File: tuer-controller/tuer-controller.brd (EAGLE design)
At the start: 46.7 x 43.2 mm, 19 parts, among them IC1 ATTINY24/44/84-PU

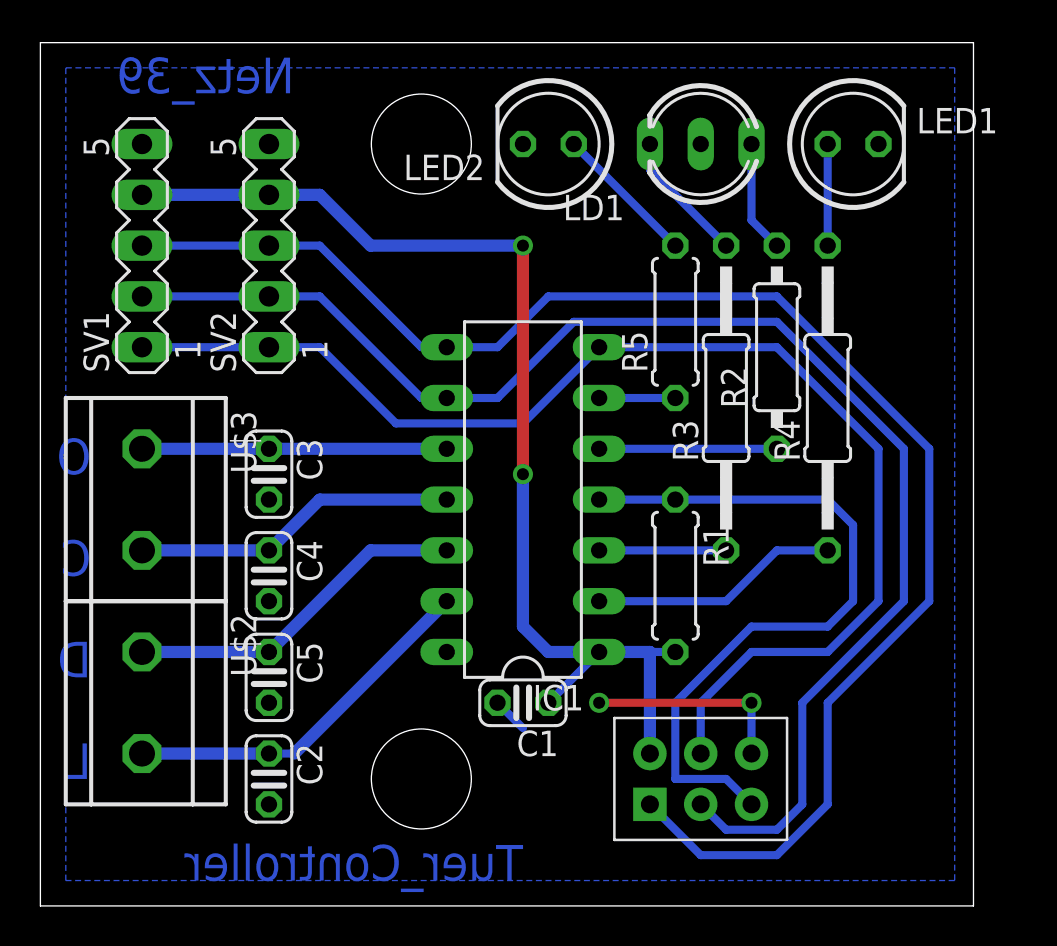
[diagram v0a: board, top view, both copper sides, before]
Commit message: Mindesgrößen der Pads und Vias angepasst
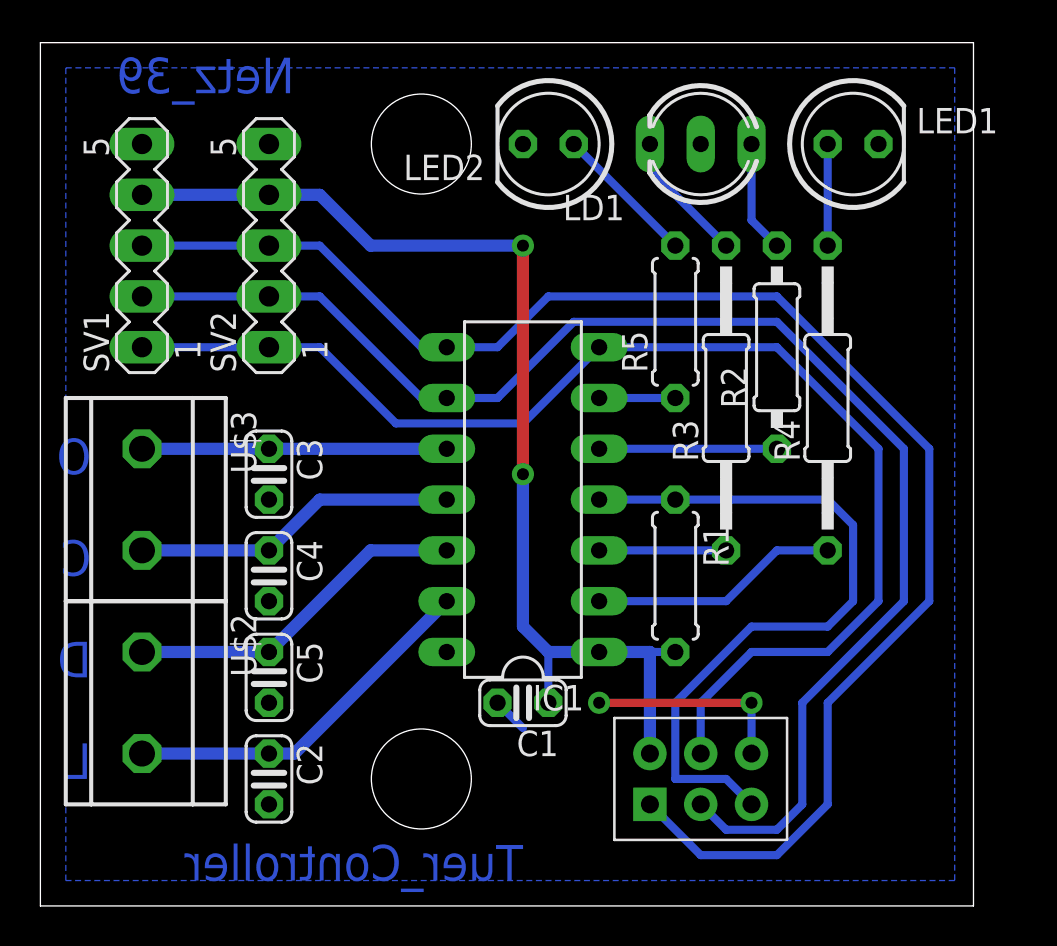
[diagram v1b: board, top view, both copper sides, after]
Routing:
- net VCC: track 56.0 -> 54.9 mm
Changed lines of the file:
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@@
 </class>
 </classes>
-<designrules name="default">
+<designrules name="default *">
 <description language="de">&lt;b&gt;EAGLE Design Rules&lt;/b&gt;
 &lt;p&gt;
@@
 <param name="mdDrill" value="8mil"/>
 <param name="mdSmdStop" value="0mil"/>
-<param name="msWidth" value="10mil"/>
+<param name="msWidth" value="12mil"/>
 <param name="msDrill" value="24mil"/>
 <param name="msMicroVia" value="9.99mm"/>
@@
 <param name="rvMicroViaOuter" value="0.25"/>
 <param name="rvMicroViaInner" value="0.25"/>
-<param name="rlMinPadTop" value="10mil"/>
+<param name="rlMinPadTop" value="12mil"/>
 <param name="rlMaxPadTop" value="20mil"/>
-<param name="rlMinPadInner" value="10mil"/>
+<param name="rlMinPadInner" value="12mil"/>
 <param name="rlMaxPadInner" value="20mil"/>
-<param name="rlMinPadBottom" value="10mil"/>
+<param name="rlMinPadBottom" value="12mil"/>
 <param name="rlMaxPadBottom" value="20mil"/>
-<param name="rlMinViaOuter" value="8mil"/>
+<param name="rlMinViaOuter" value="10mil"/>
 <param name="rlMaxViaOuter" value="20mil"/>
-<param name="rlMinViaInner" value="8mil"/>
+<param name="rlMinViaInner" value="10mil"/>
 <param name="rlMaxViaInner" value="20mil"/>
 <param name="rlMinMicroViaOuter" value="4mil"/>
@@
 <wire x1="27.94" y1="12.7" x2="30.48" y2="12.7" width="0.6096" layer="16"/>
 <wire x1="30.48" y1="12.7" x2="31.75" y2="12.7" width="0.4064" layer="16"/>
-<wire x1="27.94" y1="12.7" x2="25.4" y2="10.16" width="0.4064" layer="16"/>
 <wire x1="30.48" y1="7.62" x2="30.48" y2="12.7" width="0.6096" layer="16"/>
 <wire x1="27.94" y1="12.7" x2="25.4" y2="12.7" width="0.6096" layer="16"/>
@@
 <wire x1="5.08" y1="35.56" x2="11.43" y2="35.56" width="0.6096" layer="16"/>
 <wire x1="11.43" y1="35.56" x2="13.97" y2="35.56" width="0.6096" layer="16"/>
+<wire x1="25.4" y1="10.16" x2="25.4" y2="12.7" width="0.4064" layer="16"/>
 </signal>
 <signal name="MISO">
@@
 <wire x1="5.08" y1="7.62" x2="11.43" y2="7.62" width="0.6096" layer="16"/>
 <wire x1="20.32" y1="15.24" x2="12.7" y2="7.62" width="0.6096" layer="16"/>
-<wire x1="12.7" y1="7.62" x2="11.43" y2="7.62" width="0.4064" layer="16"/>
+<wire x1="12.7" y1="7.62" x2="11.43" y2="7.62" width="0.6096" layer="16"/>
 </signal>
 <signal name="OPEN">

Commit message: Tür-Controller: Taster für Not-Auf und Space-Pause (gemäß Workshop zur Schließanlage)
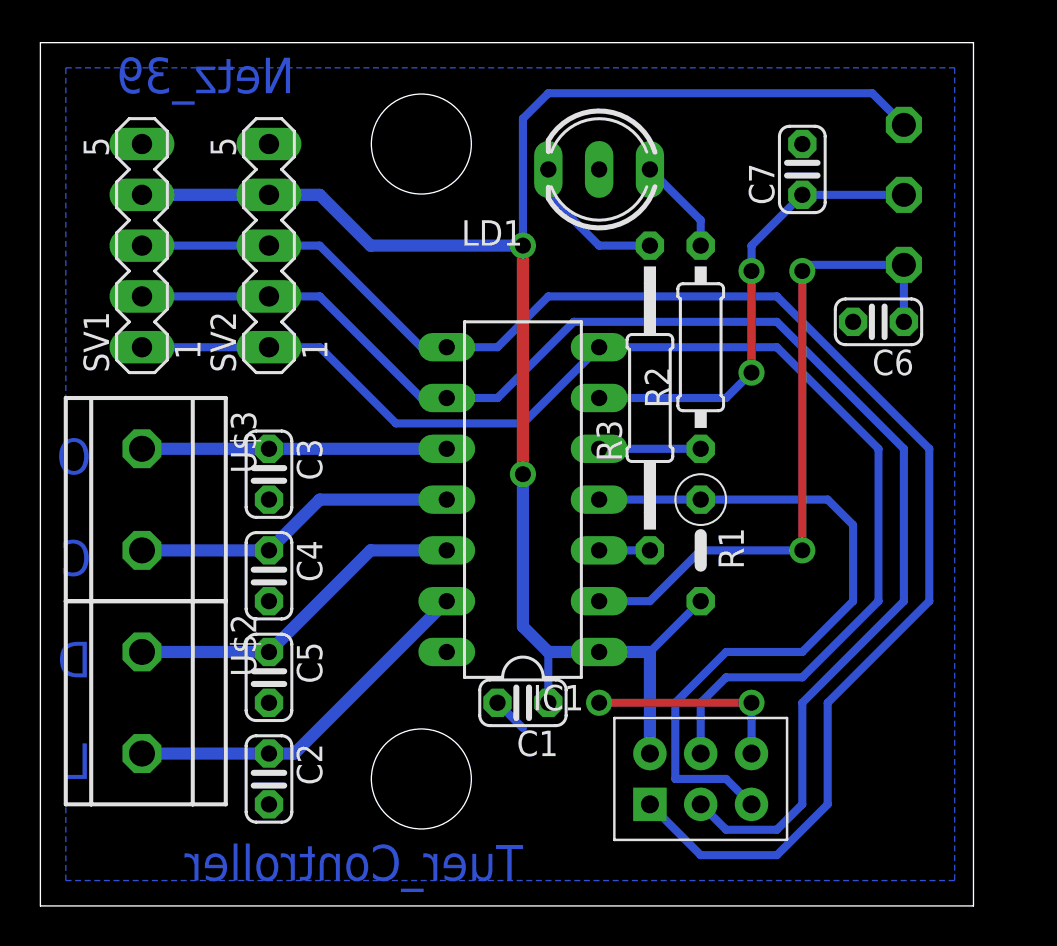
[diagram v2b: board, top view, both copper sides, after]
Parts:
- removed LED1, LED2: (no value), led:LED5MM
- removed R4: 150R, resistor:0207/15
- removed R5: 150R, resistor:0207/7
- added C6, C7: 100n, resistor:C025-024X044
- added U$5: RIACON_59_3, n39:RIACON_59_3
- R1: device resistor:0207/7 -> resistor:0207/5V
- moved LD1 5.24 mm to (27.9, 36.8)
- moved R3 3.81 mm to (30.5, 25.4)
- moved R2 3.81 mm to (33.0, 27.9)
- moved R1 1.80 mm to (33.0, 17.8)
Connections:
- removed net N$10: LED2.A, R5.2
- removed net N$11: IC1.2, R4.1
- removed net N$12: IC1.6, R5.1
- removed net N$9: LED1.A, R4.2
- new net FORCE_OPEN: C6.1, IC1.2, U$5.3
- new net PAUSE: C7.1, IC1.6, U$5.2
- net GND: now also C6.2, C7.2; no longer LED1.K, LED2.K
- net VCC: now also U$5.1
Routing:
- net FORCE_OPEN: track 0.00 -> 33.2 mm, vias 0 -> 2
- net VCC: track 54.9 -> 83.8 mm
- net PAUSE: track 0.00 -> 23.2 mm, vias 0 -> 2
- net N$11: track 12.5 -> 0.00 mm
- net N$10: track 7.18 -> 0.00 mm
- net N$9: track 5.08 -> 0.00 mm
- net N$2: track 6.35 -> 2.54 mm
- net N$12: track 3.81 -> 0.00 mm
- net N$1: track 8.89 -> 5.08 mm
- net N$3: track 5.61 -> 4.86 mm
- net N$4: track 6.66 -> 7.40 mm

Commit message: Beschriftung und Bohrlöcher
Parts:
- added U$4, U$6: (no value), holes:3,2
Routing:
- net GND: track 12.0 -> 10.2 mm
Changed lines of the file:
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@@
 <wire x1="46.66" y1="43.17" x2="0" y2="43.17" width="0" layer="20"/>
 <wire x1="0" y1="43.17" x2="0" y2="0" width="0" layer="20"/>
-<hole x="19.05" y="38.1" drill="5"/>
-<hole x="19.05" y="6.35" drill="5"/>
 <text x="2.54" y="21.59" size="1.778" layer="16" font="vector" rot="MR0">O</text>
 <text x="2.54" y="16.51" size="1.778" layer="16" font="vector" rot="MR0">C</text>
@@
 <attribute name="REICHELT" value="AKL 059-03" x="43.18" y="35.56" size="1.778" layer="28" rot="MR270" display="off"/>
 </element>
+<element name="U$4" library="holes" package="3,2" value="" x="19" y="38"/>
+<element name="U$6" library="holes" package="3,2" value="" x="19" y="6.5"/>
 </elements>
 <signals>
@@
 <wire x1="35.56" y1="10.16" x2="27.94" y2="10.16" width="0.4064" layer="1"/>
 <via x="27.94" y="10.16" extent="1-16" drill="0.8" shape="square"/>
-<wire x1="24.13" y1="8.89" x2="22.86" y2="10.16" width="0.4064" layer="16"/>
 <polygon width="0.4064" layer="16" isolate="0.3048">
 <vertex x="1.27" y="41.91"/>
